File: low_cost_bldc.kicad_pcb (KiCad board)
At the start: 4 copper layers, 40 x 40 mm, 79 parts, among them P1 USB_C_Plug_USB2.0, Q1 HSCB3014, Q2 HSCB3014, Q3 HSCB3014, Q4 HSCB3014, Q5 HSCB3014, Q6 HSCB3014, U1 CH32V003FxPx, U2 MT6701CT, U3 U2115C, U4 COS8051, U5 U2115C, U6 COS8051, U7 U2115C, U8 COS8051

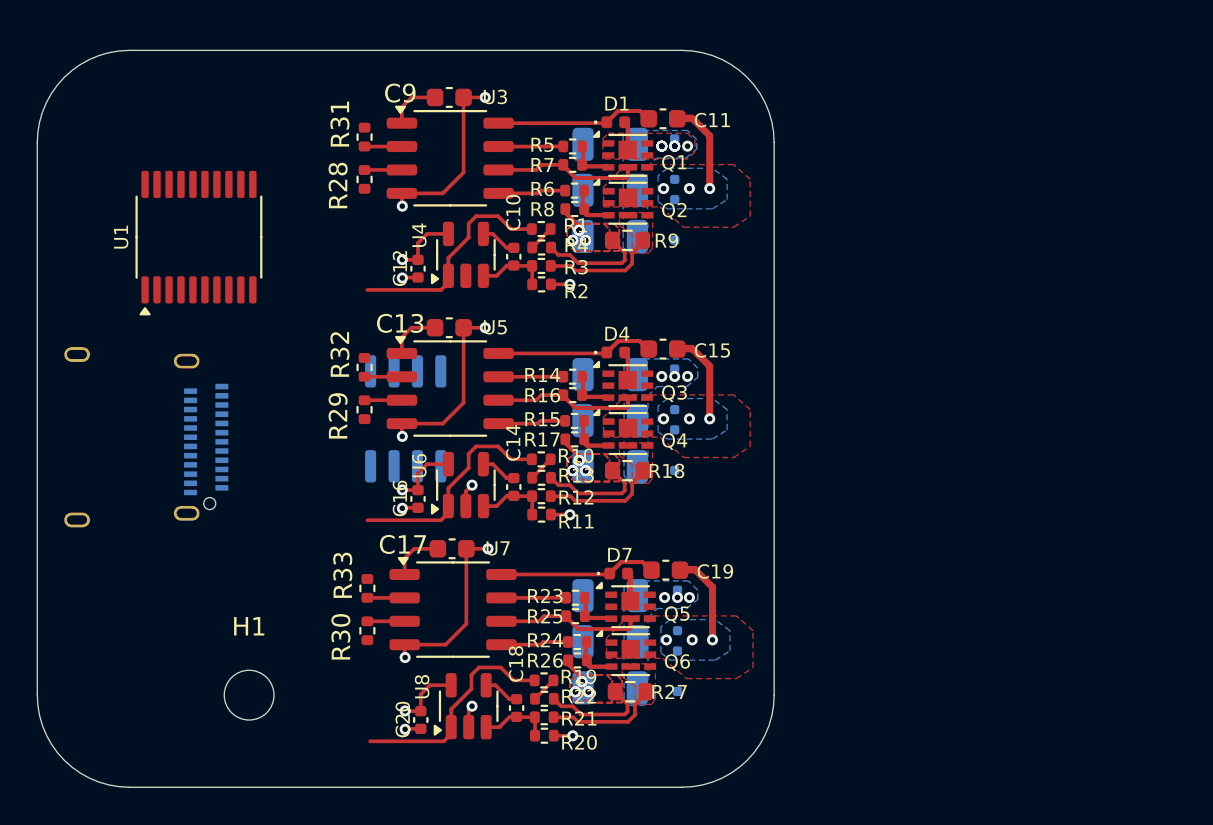
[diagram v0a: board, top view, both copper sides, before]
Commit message: Rough sketch-up of idea. Does introduce the problem of cooling the FETs now...
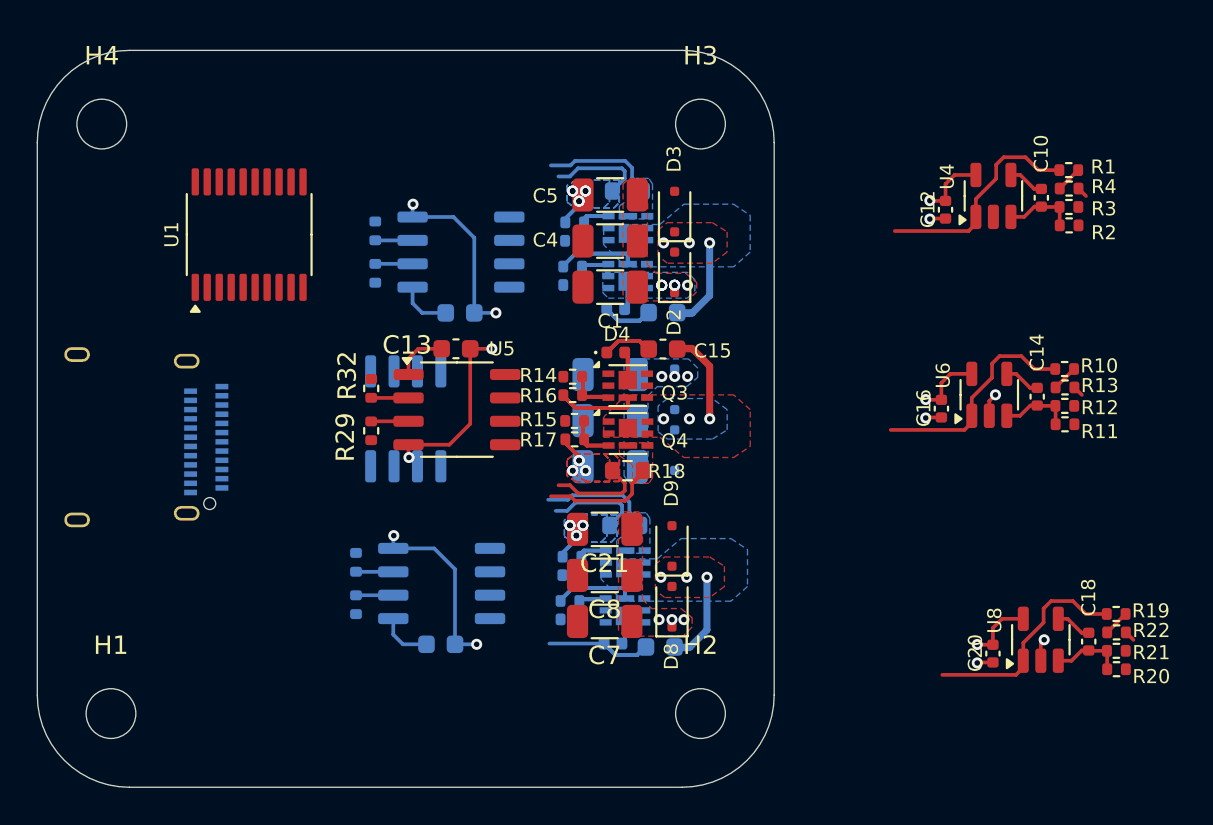
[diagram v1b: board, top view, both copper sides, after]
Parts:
- added H2: MountingHole, MountingHole:MountingHole_2.7mm_M2.5, F.Cu at (271.0, 176.0)
- added H3: MountingHole, MountingHole:MountingHole_2.7mm_M2.5, F.Cu at (271.0, 144.0)
- added H4: MountingHole, MountingHole:MountingHole_2.7mm_M2.5, F.Cu at (238.5, 144.0)
- C1, C21, C4, C5, C7, C8, D2, D3, D8, D9: moved to F.Cu
- C11, C17, C19, C9, D1, D7, Q1, Q2, Q5, Q6, R23, R24, R25, R26, R27, R28, R30, R31, R33, R5, R6, R7, R8, R9, U3, U7: moved to B.Cu
- moved C18 31.3 mm to (292.1, 172.1)
- moved C20 31.3 mm to (286.9, 172.7)
- moved R19 31.3 mm to (293.6, 170.6)
- moved R20 31.3 mm to (293.6, 173.6)
- moved R21 31.3 mm to (293.6, 172.6)
- moved R22 31.3 mm to (293.6, 171.6)
- moved U8 31.3 mm to (289.5, 172.0)
- moved U6 28.8 mm to (286.7, 158.7)
- moved C16 28.8 mm to (284.1, 159.4)
- moved C14 28.8 mm to (289.3, 158.8)
- moved R10 28.8 mm to (290.8, 157.3)
- moved R11 28.8 mm to (290.8, 160.3)
- moved R12 28.8 mm to (290.8, 159.3)
- moved R13 28.8 mm to (290.8, 158.3)
- moved C12 28.8 mm to (284.3, 148.7)
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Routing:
- net Net-(D1-K): track 13.7 -> 7.92 mm
- net Net-(D4-K): track 13.7 -> 7.92 mm
- net Net-(U3-LO): track 3.68 -> 0.00 mm
- net Net-(U5-LO): track 3.68 -> 0.00 mm
- net Net-(U7-LO): track 3.68 -> 0.00 mm
- net /PHASE_U: track 18.2 -> 14.6 mm
- net /PHASE_V: track 18.2 -> 14.6 mm
- net /PHASE_W: track 18.2 -> 14.6 mm
- net Net-(U7-HO): track 3.52 -> 0.00 mm
- net Net-(U5-HO): track 3.52 -> 0.00 mm
- net Net-(U3-HO): track 3.52 -> 0.00 mm
- net GND: track 63.9 -> 60.8 mm, vias 32 -> 29
- net Net-(D7-K): track 13.7 -> 10.9 mm
- added copper zone on B.Cu, net GND
- added copper zone on B.Cu, net Net-(Q2-S-Pad4)
- added copper zone on B.Cu, net Net-(Q6-S-Pad4)
- removed copper zone on F.Cu, net Net-(Q2-S-Pad4)
- removed copper zone on F.Cu, net Net-(Q6-S-Pad4)
